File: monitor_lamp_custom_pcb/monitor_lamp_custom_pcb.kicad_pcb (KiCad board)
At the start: 2 copper layers, 32 parts, among them IC1 HUSB238, J2 VEML7700_Connection, J3 LD2410C_Connection, J4 Conn_01x02, Q1 AO3401A, Q2 IRLZ44N, U1 TPS563300, U2 TPS561208DDCT, U3 ESP32-C3_SUPERMINI_TH, U4 MAX40200AUK

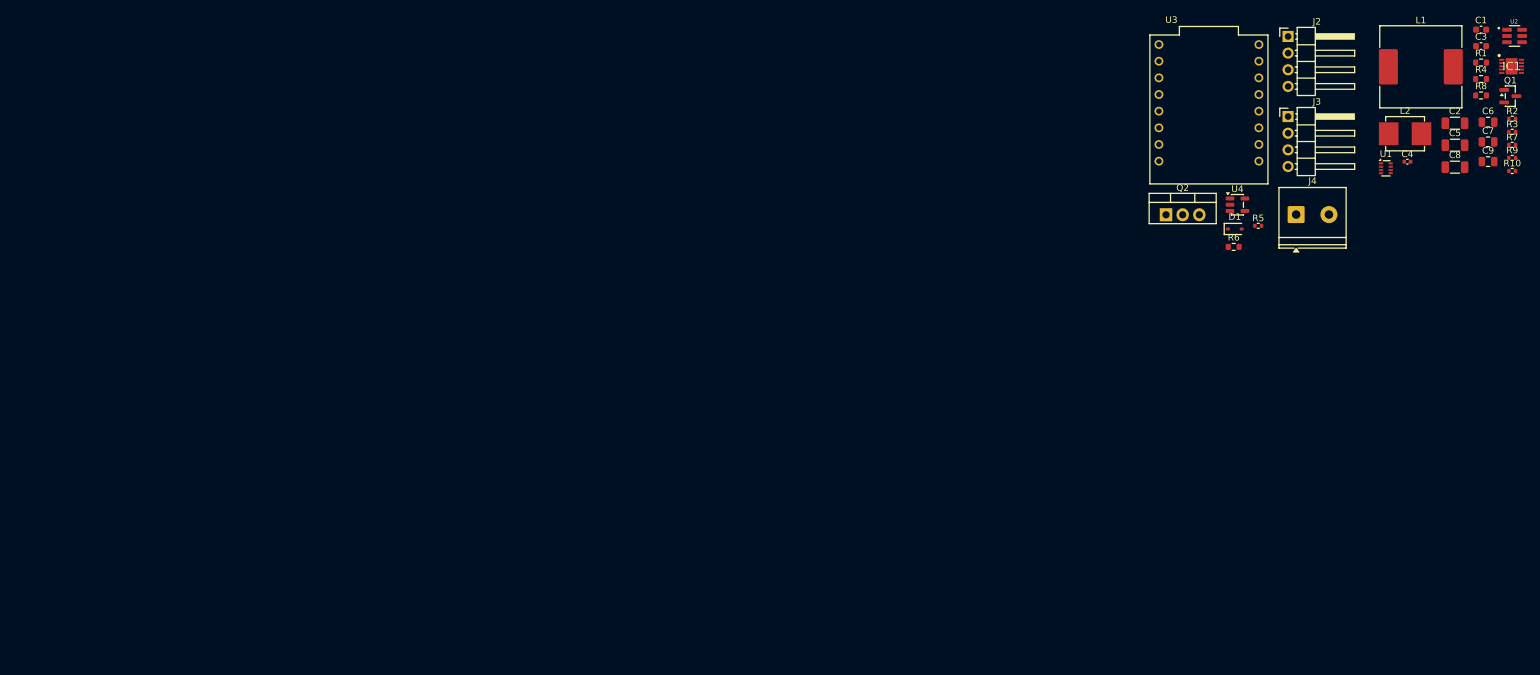
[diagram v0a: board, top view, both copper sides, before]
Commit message: Started to place component in the pcb design.
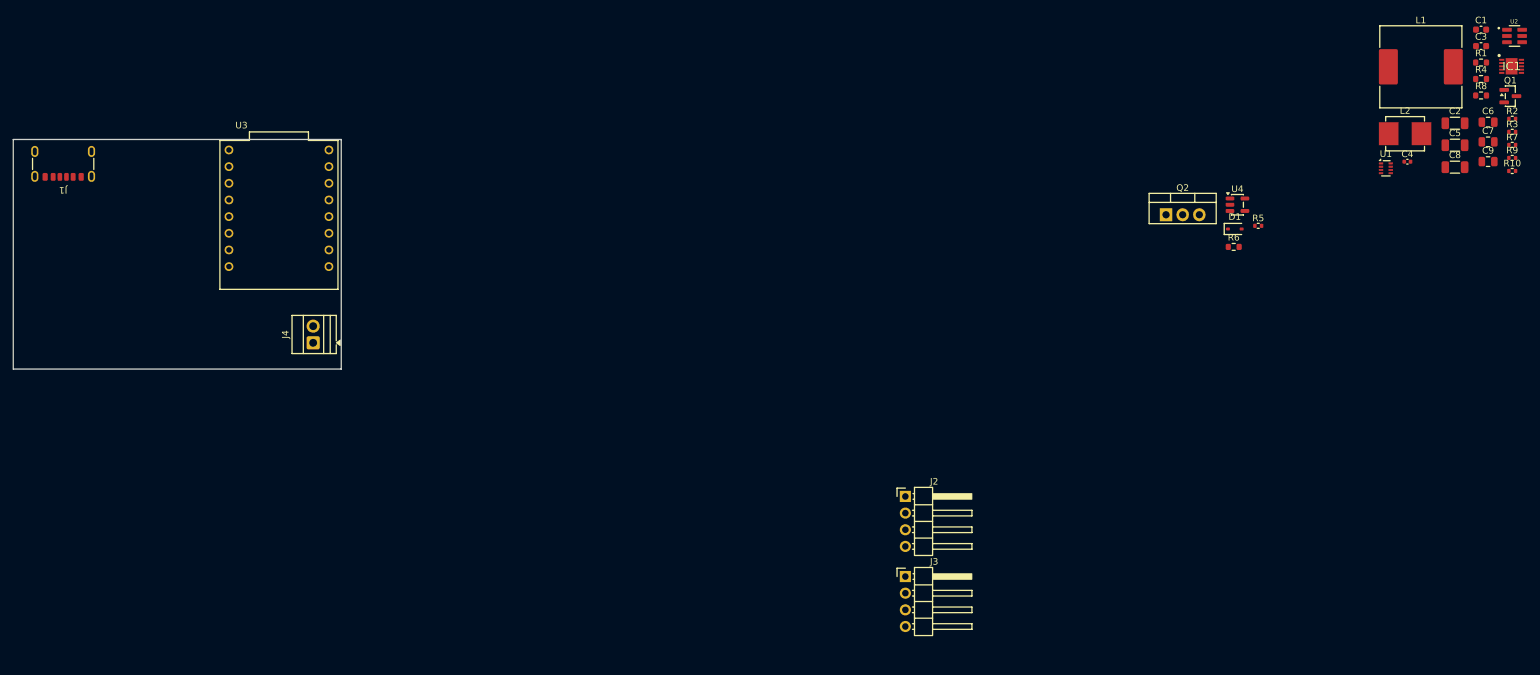
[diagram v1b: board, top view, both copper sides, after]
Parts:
- added J1: USB_C_Receptacle_PowerOnly_6P, Connector_USB:USB_C_Receptacle_GCT_USB4125-xx-x_6P_TopMnt_Horizontal, F.Cu at (49.6, 42.6)
- J4: footprint TerminalBlock_Phoenix:TerminalBlock_Phoenix_PT-1,5-2-5.0-H_1x02_P5.00mm_Horizontal -> TerminalBlock:TerminalBlock_Xinya_XY308-2.54-2P_1x02_P2.54mm_Horizontal
- moved J4 151.1 mm to (87.7, 71.0), turned to 90 degrees
- moved U3 142.7 mm to (82.5, 51.5)
- moved J2 91.2 mm to (178.0, 94.4)
- moved J3 91.2 mm to (178.0, 106.6)
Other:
- board outline added: 50 x 35 mm

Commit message: Started to place components on the board layout
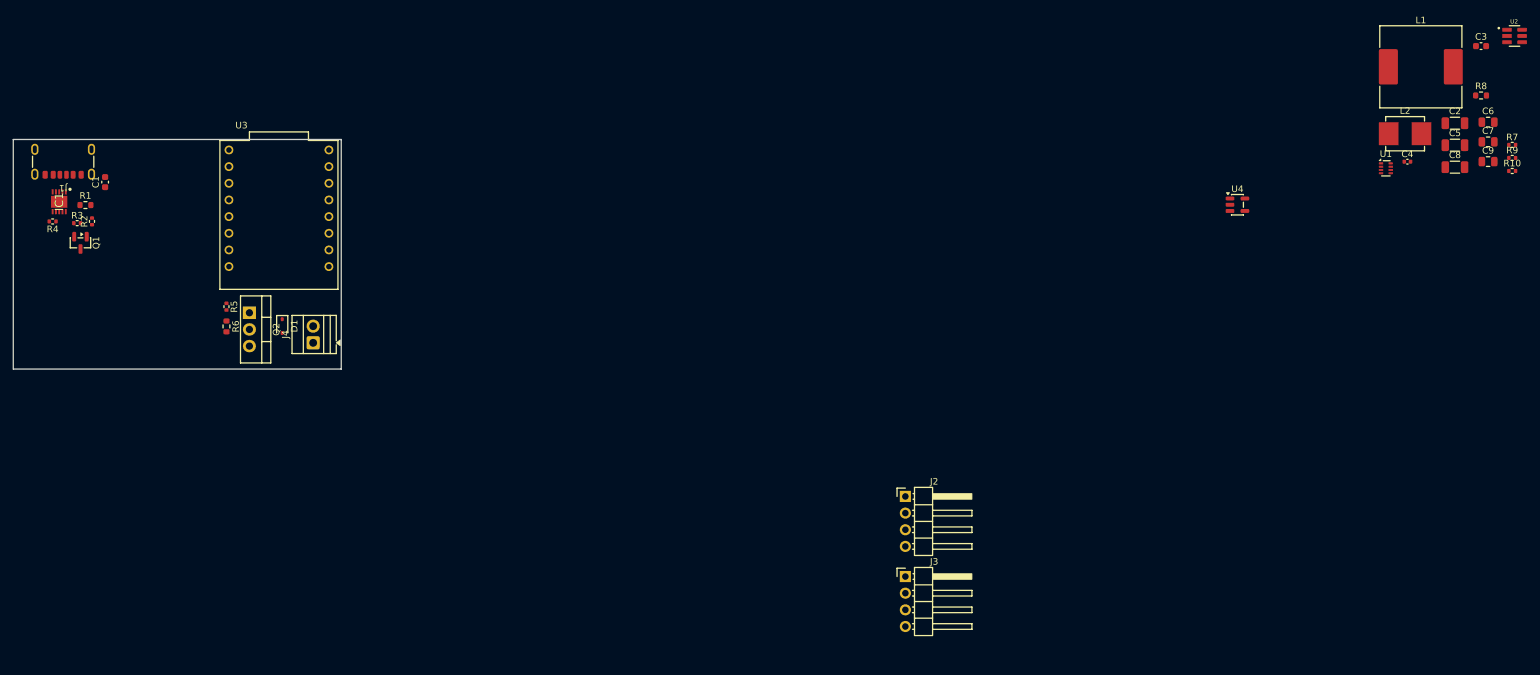
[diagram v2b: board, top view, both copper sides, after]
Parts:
- R4: footprint Resistor_SMD:R_0603_1608Metric -> Resistor_SMD:R_0402_1005Metric
- moved IC1 222.4 mm to (49.0, 49.5), turned to -90 degrees
- moved R3 219.2 mm to (51.7, 52.8)
- moved Q1 219.1 mm to (52.2, 55.8), turned to -90 degrees
- moved R4 218.8 mm to (48.0, 52.5), turned to 180 degrees
- moved R2 217.1 mm to (54.0, 52.5), turned to 90 degrees
- moved R1 213.9 mm to (53.0, 50.0)
- moved C1 211.0 mm to (56.0, 46.5), turned to 90 degrees
- moved R5 157.8 mm to (74.5, 65.5), turned to -90 degrees
- moved R6 154.0 mm to (74.5, 68.5), turned to -90 degrees
- moved D1 146.0 mm to (83.0, 68.5), turned to -90 degrees
- moved Q2 140.5 mm to (78.0, 66.4), turned to -90 degrees
- moved J1 0.33 mm to (49.6, 42.3)
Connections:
- U3 pad 2: PWM_Control -> unconnected-(U3-GPIO2-Pad2)
- U3 pad 21: unconnected-(U3-GPIO21-Pad21) -> PWM_Control

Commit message: Added almost all components to the board. Next step trace
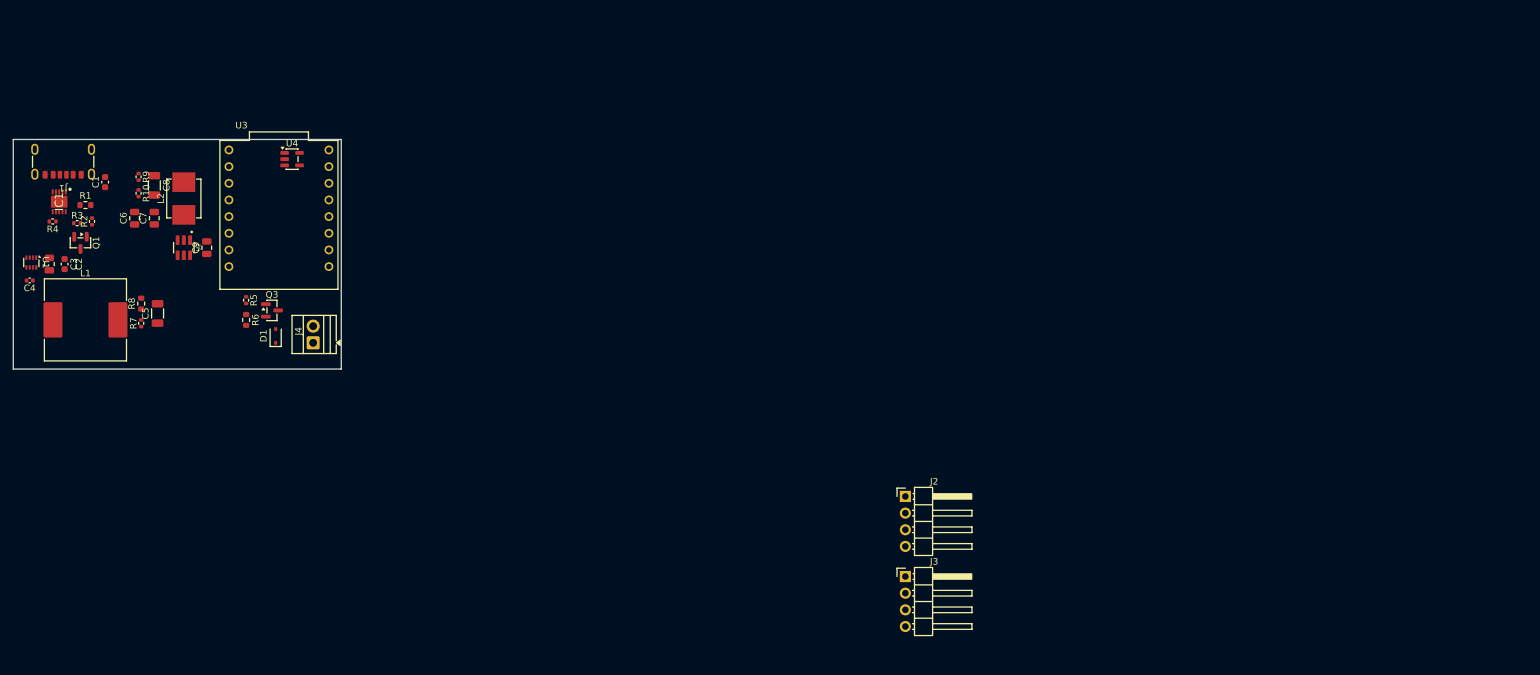
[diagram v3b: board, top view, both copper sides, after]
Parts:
- removed Q2: IRLZ44N, Package_TO_SOT_THT:TO-220-3_Vertical
- added Q3: AO3400A, Package_TO_SOT_SMD:SOT-23, F.Cu at (81.4, 66.1)
- C2: footprint Capacitor_SMD:C_1206_3216Metric -> Capacitor_SMD:C_0805_2012Metric
- moved C3 218.5 mm to (49.8, 59.0), turned to -90 degrees
- moved C2 215.4 mm to (47.5, 59.0), turned to -90 degrees
- moved C4 210.8 mm to (44.5, 61.5), turned to 180 degrees
- moved R7 210.8 mm to (61.5, 68.0), turned to 90 degrees
- moved R10 209.4 mm to (61.1, 48.2), turned to -90 degrees
- moved R9 209.4 mm to (61.1, 45.7), turned to -90 degrees
- moved L1 207.2 mm to (53.0, 67.5)
- moved U1 207.0 mm to (44.8, 58.8), turned to -90 degrees
- moved C6 206.9 mm to (60.5, 52.0), turned to 90 degrees
- moved R8 206.7 mm to (61.5, 65.0), turned to 90 degrees
- moved U2 205.4 mm to (68.0, 56.5), turned to -90 degrees
- moved C7 203.7 mm to (63.5, 52.0), turned to 90 degrees
- moved C5 199.4 mm to (64.0, 66.5), turned to 90 degrees
- moved C8 198.3 mm to (63.5, 47.0), turned to -90 degrees
- moved C9 195.8 mm to (71.5, 56.5), turned to 90 degrees
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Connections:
- J4 pad 1: Net-(D1-A) -> /+12V
- J4 pad 2: /+12V -> Net-(D1-A)
- U1 pad 2: unconnected-(U1-EN-Pad2) -> /+15V

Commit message: Placed all components, changed the J2 & J3 connectors
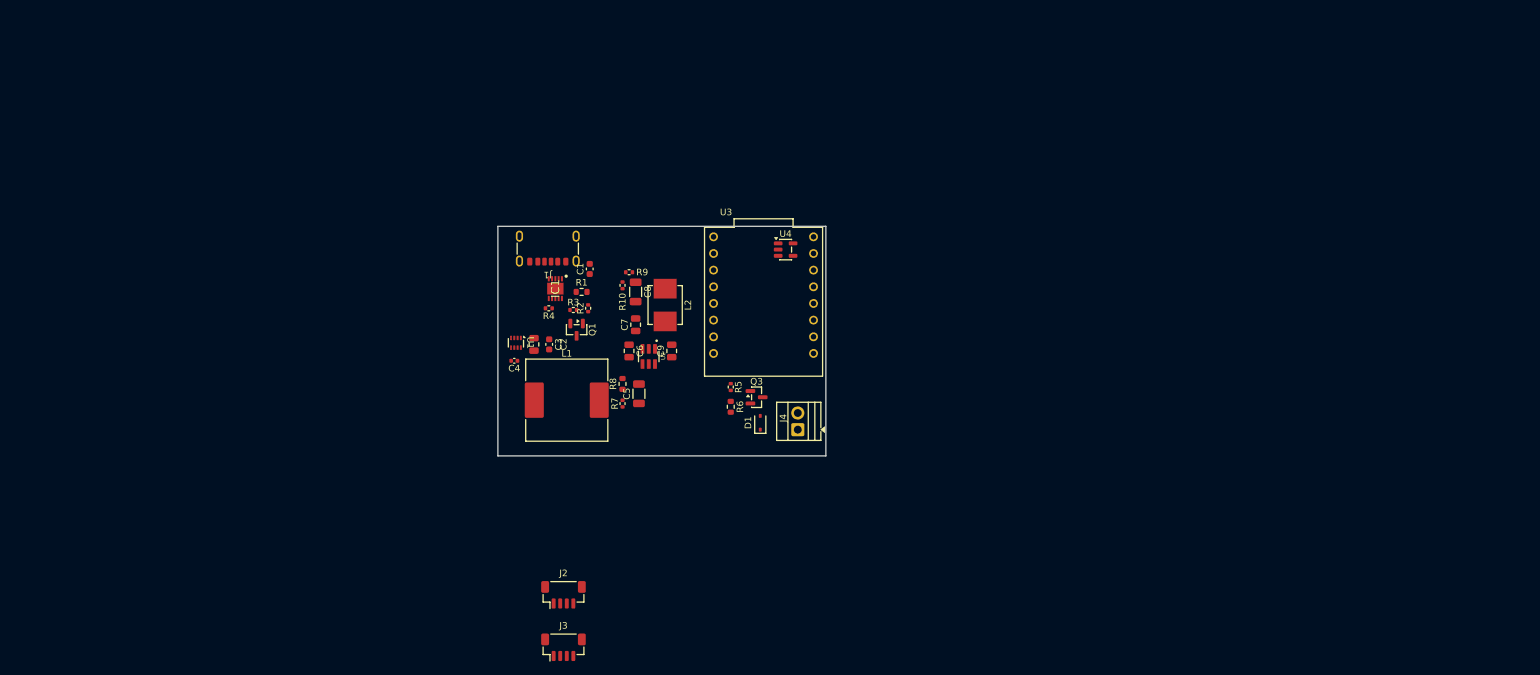
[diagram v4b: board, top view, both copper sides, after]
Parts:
- J2, J3: footprint Connector_PinHeader_2.54mm:PinHeader_1x04_P2.54mm_Horizontal -> Connector_JST:JST_SH_BM04B-SRSS-TB_1x04-1MP_P1.00mm_Vertical
- moved C6 78.1 mm to (135.9, 72.2), turned to -90 degrees
- moved IC1 76.8 mm to (124.6, 62.7)
- moved R4 76.8 mm to (123.6, 65.7)
- moved Q1 76.8 mm to (127.9, 69.0)
- moved R1 76.8 mm to (128.6, 63.2)
- moved R2 76.8 mm to (129.6, 65.7)
- moved R3 76.8 mm to (127.4, 66.0)
- moved U4 76.5 mm to (159.7, 56.8)
- moved R9 76.2 mm to (135.9, 60.2), turned to 180 degrees
- moved C7 75.2 mm to (136.9, 68.2)
- moved C8 75.2 mm to (136.9, 63.2)
- moved L2 75.2 mm to (141.4, 65.2)
- moved R10 75.1 mm to (134.9, 62.2)
- moved C1 75.1 mm to (129.9, 59.7)
- moved D1 75.1 mm to (155.9, 83.2)
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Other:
- copper layers 2 -> 4

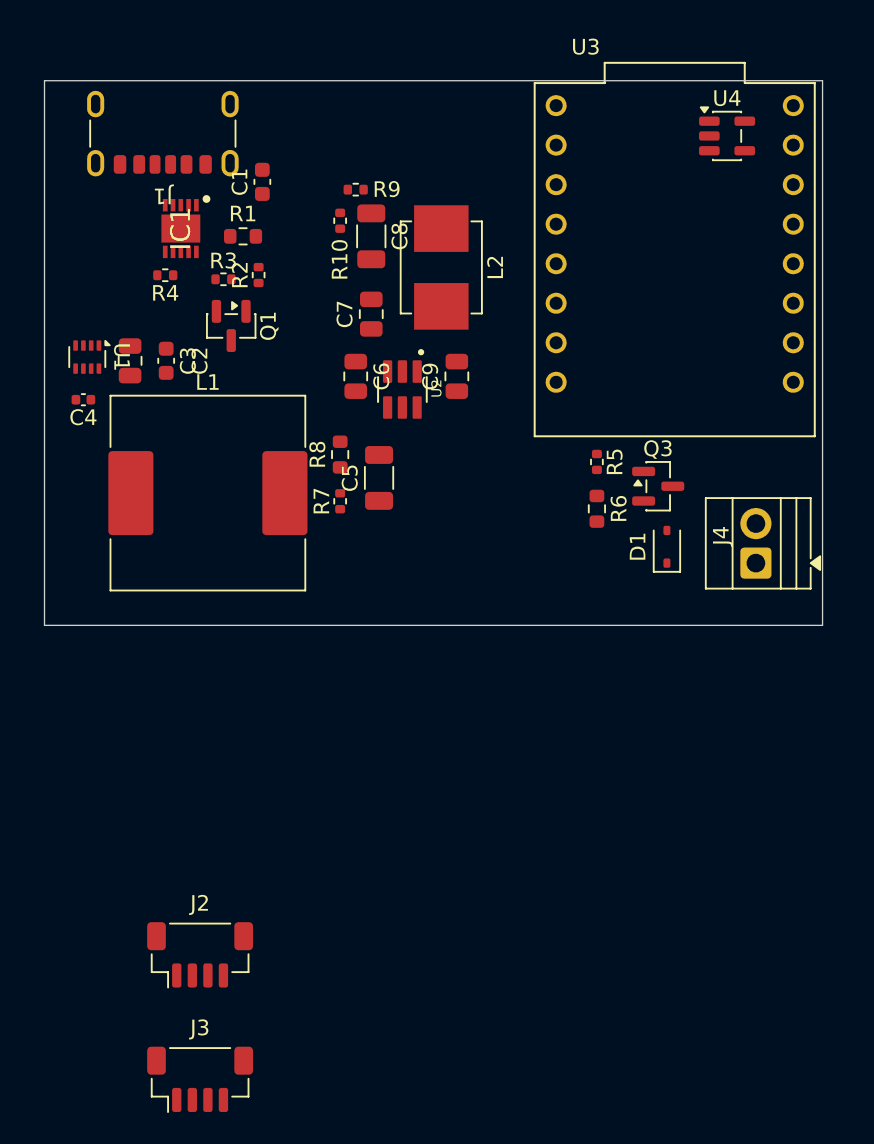
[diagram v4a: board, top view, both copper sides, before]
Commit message: Modified layout and J2&J3 connectors
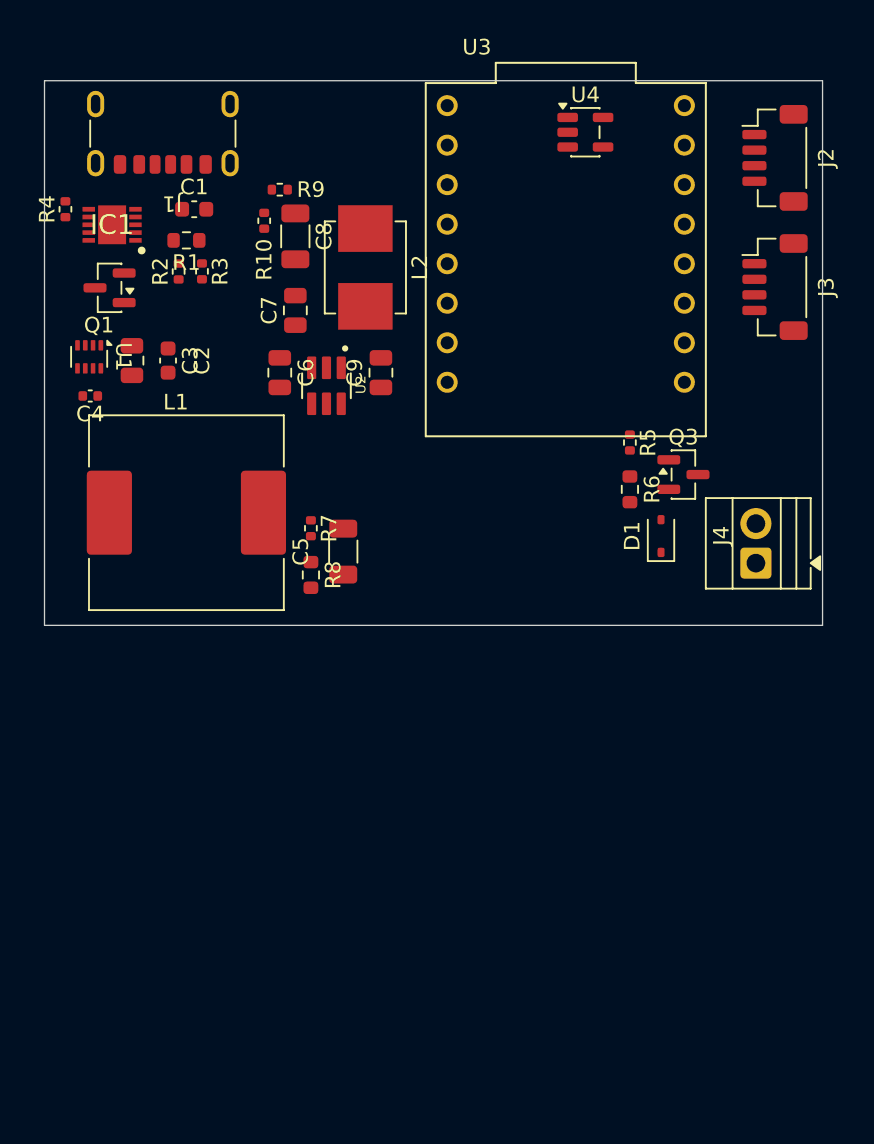
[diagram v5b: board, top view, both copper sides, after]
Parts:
- moved J2 63.1 mm to (162.8, 58.2), turned to -90 degrees
- moved J3 62.9 mm to (162.8, 66.5), turned to -90 degrees
- moved U4 9.11 mm to (150.6, 56.5)
- moved Q1 8.19 mm to (120.1, 66.5), turned to 180 degrees
- moved R8 7.96 mm to (133.0, 85.0), turned to -90 degrees
- moved R4 7.69 mm to (117.2, 61.5), turned to 90 degrees
- moved U3 7.00 mm to (149.4, 64.7)
- moved C5 5.26 mm to (135.1, 83.5), turned to -90 degrees
- moved R2 5.15 mm to (124.5, 65.5)
- moved C6 4.89 mm to (131.0, 72.0)
- moved C7 4.89 mm to (132.0, 68.0)
- moved C9 4.89 mm to (137.5, 72.0)
- moved U2 4.89 mm to (134.0, 72.8)
- moved C8 4.88 mm to (132.0, 63.2)
- moved L2 4.88 mm to (136.5, 65.2)
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
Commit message: Selected 4-Layer setup. Started to trace
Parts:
- moved J4 15.6 mm to (146.0, 83.5)
- moved Q3 15.6 mm to (141.3, 77.8)
- moved R5 15.6 mm to (137.9, 75.8)
- moved R6 15.6 mm to (137.9, 78.8)
- moved D1 15.0 mm to (140.5, 81.5)
- moved U3 0.50 mm to (149.9, 64.7)
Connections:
- IC1 pad 11: unconnected-(IC1-GND-Pad11) -> GND
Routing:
- net /ESP32_Sensors_Mosfet/SCL: track 0.00 -> 21.8 mm
- net /ESP32_Sensors_Mosfet/SDA: track 0.00 -> 21.2 mm
- net Net-(IC1-GATE): track 0.00 -> 8.64 mm
- net Net-(J3-Pin_2): track 0.00 -> 6.64 mm
- net PWM_Control: track 0.00 -> 5.44 mm
- net Net-(IC1-CC1): track 0.00 -> 4.96 mm
- net Net-(J3-Pin_3): track 0.00 -> 4.83 mm
- net Net-(IC1-CC2): track 0.00 -> 4.00 mm
- net Net-(IC1-VSET): track 0.00 -> 1.70 mm
- added copper zone on In1.Cu, net GND
